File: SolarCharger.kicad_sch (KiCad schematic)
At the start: 28 parts, among them U5 ADM1176-1ARMZ-R7

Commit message: Local Stash
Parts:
- added R118: 0R, Resistor_SMD:R_0603_1608Metric, symbol Device:R_Small
- R56: value 0R -> 150k; MPN C844915 -> C402995
- R57: now not fitted; now left out of the parts list
- R58: value 126k -> 100k; now not fitted; now left out of the parts list
- R59: value 1.91M -> 2.32M
- R60: value 182k -> 143k
- R62: value 1.47M -> 2M
- R63: value 200k -> 270k
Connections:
- net MPPT/VCC: now also R118.1
- net MPPT/MPPC renamed MPPC
- net MPPC: now also R118.2
- no-connect marks 2 -> 1
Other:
- note added: "DNP if using MPPC"
- note added: "I2C ADDR R55, R56 +Z: DNP, 150k: 0x46"
- note added: "V_in(mppc) = 1.00 * (1 + R57 / R58) V_in(mppc) = 1.00 * (1 + 1.91M / 100k) V_in(mppc) = 1.00 * (1 + 19.1) V_in(mppc) = 20.1V"
- note added: "V_in(turnon) = 1.05 * (1 + R59 / R60) V_in(turnon) = 1.05 * (1 + 2.32M / 143k) V_in(turnon) = 1.05 * (1 + 16.22) V_in(turnon) = 18.08V"
- note added: "V_out = 1.00 * (1 + R62 / R63) V_out = 1.00 * (1 + 2M / 270k) V_out = 1.00 * (1 + 7.41) V_out = 8.41V"
- note removed: "I2C ADDR R55, R56 +Z: DNP, 0R: 0x42 Translated: 0x62"
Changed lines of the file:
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@@
 		(comment 2 "V. Kumar")
 	)
+	(text "V_in(mppc) = 1.00 * (1 + R57 / R58)\nV_in(mppc) = 1.00 * (1 + 1.91M / 100k)\nV_in(mppc) = 1.00 * (1 + 19.1)\nV_in(mppc) = 20.1V"
+		(exclude_from_sim no)
+		(at 18.288 94.996 0)
+		(effects
+			(font
+				(size 1.27 1.27)
+			)
+			(justify left)
+		)
+	)
 	(text "#TODO: Spec Fuses"
 		(exclude_from_sim no)
@@
 		)
 	)
+	(text "V_in(turnon) = 1.05 * (1 + R59 / R60)\nV_in(turnon) = 1.05 * (1 + 2.32M / 143k)\nV_in(turnon) = 1.05 * (1 + 16.22)\nV_in(turnon) = 18.08V"
+		(exclude_from_sim no)
+		(at 18.542 137.16 0)
+		(effects
+			(font
+				(size 1.27 1.27)
+			)
+			(justify left)
+		)
+	)
 	(text "Rsense"
 		(exclude_from_sim no)
@@
 		)
 	)
+	(text "V_out = 1.00 * (1 + R62 / R63)\nV_out = 1.00 * (1 + 2M / 270k)\nV_out = 1.00 * (1 + 7.41)\nV_out = 8.41V"
+		(exclude_from_sim no)
+		(at 116.84 116.586 0)
+		(effects
+			(font
+				(size 1.27 1.27)
+			)
+			(justify left)
+		)
+	)
 	(text "#TODO: Check Resistor Values"
 		(exclude_from_sim no)
@@
 		)
 	)
-	(text "I2C ADDR\nR55, R56\n+Z: DNP, 0R: 0x42\nTranslated: 0x62"
+	(text "DNP if using MPPC"
+		(exclude_from_sim no)
+		(at 93.726 125.73 0)
+		(effects
+			(font
+				(size 0.889 0.889)
+			)
+		)
+	)
+	(text "I2C ADDR\nR55, R56\n+Z: DNP, 150k: 0x46"
 		(exclude_from_sim no)
 		(at 181.356 91.948 0)
@@
 		(at 248.92 54.61)
 	)
-	(no_connect
-		(at 86.36 119.38)
-	)
 	(wire
 		(pts
@@
 	(wire
 		(pts
+			(xy 86.36 119.38) (xy 90.17 119.38)
+		)
+		(stroke
+			(width 0)
+			(type default)
+		)
+	)
+	(wire
+		(pts
 			(xy 133.35 53.34) (xy 133.35 59.69)
 		)
@@
 	(wire
 		(pts
+			(xy 95.25 119.38) (xy 100.33 119.38)
+		)
+		(stroke
+			(width 0)
+			(type default)
+		)
+	)
+	(wire
+		(pts
 			(xy 74.93 130.81) (xy 78.74 130.81)
 		)
@@
 		)
 	)
+	(label "MPPC"
+		(at 100.33 119.38 180)
+		(effects
+			(font
+				(size 0.889 0.889)
+			)
+			(justify right bottom)
+		)
+	)
 	(label "A1"
 		(at 243.84 78.74 180)
@@
 		)
 	)
+	(label "MPPC"
+		(at 54.61 111.76 0)
+		(effects
+			(font
+				(size 0.889 0.889)
+			)
+			(justify left bottom)
+		)
+	)
 	(label "PGOOD"
 		(at 86.36 105.41 0)
@@
 			)
 		)
-		(property "Value" "0R"
+		(property "Value" "150k"
 			(at 237.3479 84.968 0)
 			(effects
@@
 			)
 		)
-		(property "MPN" "C844915"
+		(property "MPN" "C402995"
 			(at 238.76 83.82 0)
 			(effects
@@
 		(unit 1)
 		(exclude_from_sim no)
-		(in_bom yes)
+		(in_bom no)
 		(on_board yes)
-		(dnp no)
+		(dnp yes)
 		(property "Reference" "R57"
 			(at 53.34 106.934 0)
@@
 			)
 		)
-		(property "Value" "1.91M"
+		(property "Value" "2.32M"
 			(at 68.58 135.128 90)
 			(effects
@@
 			)
 		)
-		(property "Value" "182k"
+		(property "Value" "143k"
 			(at 81.28 135.128 90)
 			(effects
@@
 	)
 	(symbol
+		(lib_id "Device:R_Small")
+		(at 92.71 119.38 90)
+		(unit 1)
+		(exclude_from_sim no)
+		(in_bom yes)
+		(on_board yes)
+		(dnp no)
+		(property "Reference" "R118"
+			(at 92.71 121.666 90)
+			(effects
+				(font
+					(size 1.27 1.27)
+				)
+			)
+		)
+		(property "Value" "0R"
+			(at 92.71 123.444 90)
+			(effects
+				(font
+					(size 1.27 1.27)
+				)
+			)
+		)
+		(property "Footprint" "Resistor_SMD:R_0603_1608Metric"
+			(at 92.71 119.38 0)
+			(effects
+				(font
+					(size 1.27 1.27)
+				)
+				(hide yes)
+			)
+		)
+		(property "Datasheet" "~"
+			(at 92.71 119.38 0)
+			(effects
+				(font
+					(size 1.27 1.27)
+				)
+				(hide yes)
+			)
+		)
+		(property "Description" "Resistor, small symbol"
+			(at 92.71 119.38 0)
+			(effects
+				(font
+					(size 1.27 1.27)
+				)
+				(hide yes)
+			)
+		)
+		(property "MPN" "C237792"
+			(at 92.71 119.38 90)
+			(effects
+				(font
+					(size 1.27 1.27)
+				)
+				(hide yes)
+			)
+		)
+		(pin "1"
+		)
+		(pin "2"
+		)
+		(instances
+			(project "+Z"
+				(path "/977a45af-b6d4-4b54-8e70-e74e2c44e8e7/3495d2a7-7425-4e27-a34a-beb5018fad2a"
+					(reference "R118")
+					(unit 1)
+				)
+			)
+		)
+	)
+	(symbol
 		(lib_id "Device:Solar_Cell")
 		(at 48.26 59.69 270)
@@
 			)
 		)
-		(property "Value" "200k"
+		(property "Value" "270k"
 			(at 106.68 117.856 0)
 			(effects
@@
 		(unit 1)
 		(exclude_from_sim no)
-		(in_bom yes)
+		(in_bom no)
 		(on_board yes)
-		(dnp no)
+		(dnp yes)
 		(property "Reference" "R58"
 			(at 53.34 114.554 0)
@@
 			)
 		)
-		(property "Value" "126k"
+		(property "Value" "100k"
 			(at 53.34 116.586 0)
 			(effects
@@
 			)
 		)
-		(property "Value" "1.47M"
+		(property "Value" "2M"
 			(at 106.68 107.696 0)
 			(effects

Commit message: V4 Updates
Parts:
- added H10, H11, H12, H13, H14, H15, H16, H17, H18, H19, H20, H9: MountingHole_Pad, TestPoint:TestPoint_Pad_D1.0mm, symbol Mechanical:MountingHole_Pad
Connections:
- net GND: now also H17.1, H18.1, H19.1, H20.1, H9.1
- net at D6.1 (K), F5.2, SC6.1 (+): now also H15.1
- net at D5.1 (K), D6.2 (A), SC5.1 (+)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: now also H14.1
- net at D3.1 (K), D4.2 (A), SC3.1 (+)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: now also H12.1, H16.1
- net at D2.1 (K), D3.2 (A), SC2.1 (+)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: now also H11.1
- net at D1.1 (K), D2.2 (A), SC1.1 (+)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: now also H10.1
- net at D4.1 (K), D5.2 (A), SC4.1 (+)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: now also H13.1
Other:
- moved on the sheet: R118, R57, R58, R59, R60, R61, R62, R63

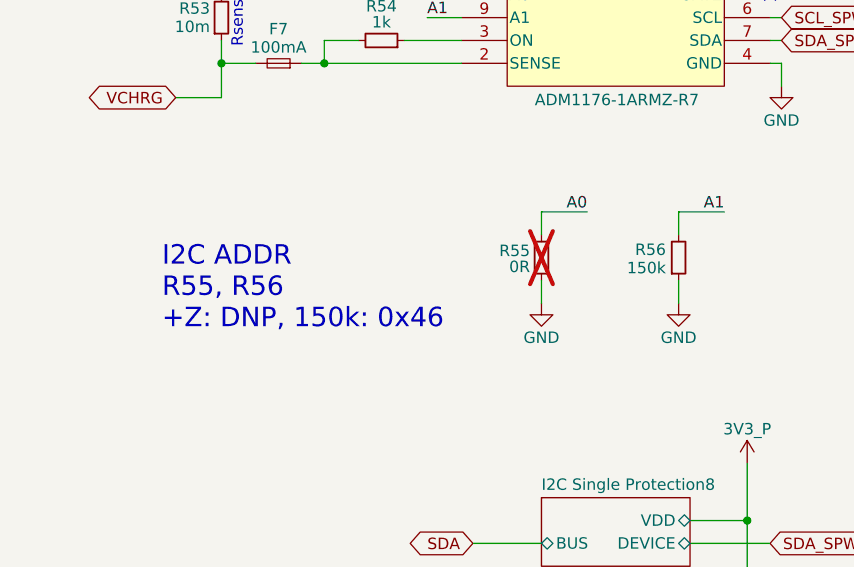
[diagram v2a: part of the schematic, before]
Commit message: Coil direction comment clarification
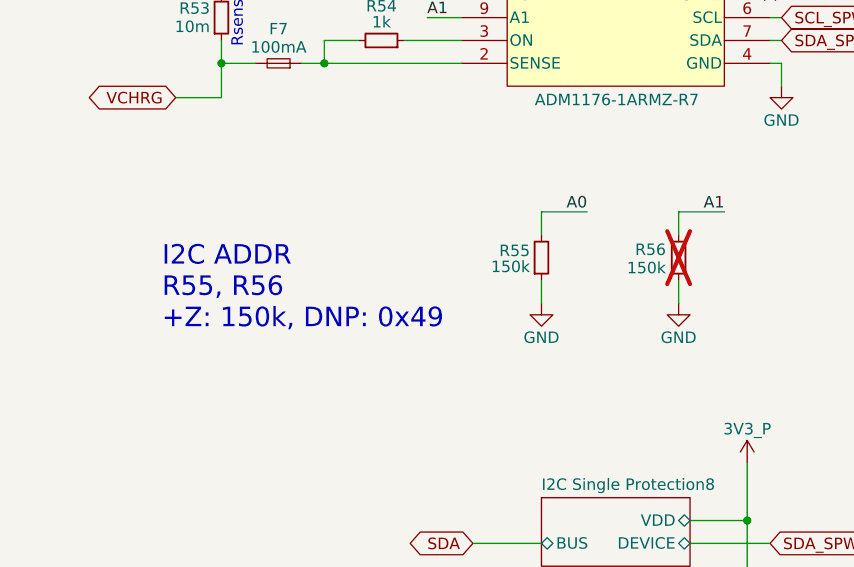
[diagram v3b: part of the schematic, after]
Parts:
- R55: value 0R -> 150k; now fitted; now in the parts list
- R56: now not fitted; now left out of the parts list
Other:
- note added: "I2C ADDR R55, R56 +Z: 150k, DNP: 0x49"
- note removed: "I2C ADDR R55, R56 +Z: DNP, 150k: 0x46"
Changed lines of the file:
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@@
 		)
 	)
-	(text "I2C ADDR\nR55, R56\n+Z: DNP, 150k: 0x46"
+	(text "I2C ADDR\nR55, R56\n+Z: 150k, DNP: 0x49"
 		(exclude_from_sim no)
 		(at 181.356 91.948 0)
@@
 		)
 		(instances
-			(project "Z+"
+			(project "+Z"
 				(path "/977a45af-b6d4-4b54-8e70-e74e2c44e8e7/3495d2a7-7425-4e27-a34a-beb5018fad2a"
 					(reference "R53")
@@
 		)
 		(instances
-			(project "Z+"
+			(project "+Z"
 				(path "/977a45af-b6d4-4b54-8e70-e74e2c44e8e7/3495d2a7-7425-4e27-a34a-beb5018fad2a"
 					(reference "#PWR057")
@@
 		)
 		(instances
-			(project "Z+"
+			(project "+Z"
 				(path "/977a45af-b6d4-4b54-8e70-e74e2c44e8e7/3495d2a7-7425-4e27-a34a-beb5018fad2a"
 					(reference "#PWR055")
@@
 		(unit 1)
 		(exclude_from_sim no)
-		(in_bom yes)
+		(in_bom no)
 		(on_board yes)
-		(dnp no)
+		(dnp yes)
 		(property "Reference" "R56"
 			(at 237.3479 82.936 0)
@@
 		)
 		(instances
-			(project "Z+"
+			(project "+Z"
 				(path "/977a45af-b6d4-4b54-8e70-e74e2c44e8e7/3495d2a7-7425-4e27-a34a-beb5018fad2a"
 					(reference "R56")
@@
 		)
 		(instances
-			(project "Z+"
+			(project "+Z"
 				(path "/977a45af-b6d4-4b54-8e70-e74e2c44e8e7/3495d2a7-7425-4e27-a34a-beb5018fad2a"
 					(reference "SC6")
@@
 		)
 		(instances
-			(project "Z+"
+			(project "+Z"
 				(path "/977a45af-b6d4-4b54-8e70-e74e2c44e8e7/3495d2a7-7425-4e27-a34a-beb5018fad2a"
 					(reference "R61")
@@
 		)
 		(instances
-			(project "Z+"
+			(project "+Z"
 				(path "/977a45af-b6d4-4b54-8e70-e74e2c44e8e7/3495d2a7-7425-4e27-a34a-beb5018fad2a"
 					(reference "#PWR042")
@@
 		)
 		(instances
-			(project "Z+"
+			(project "+Z"
 				(path "/977a45af-b6d4-4b54-8e70-e74e2c44e8e7/3495d2a7-7425-4e27-a34a-beb5018fad2a"
 					(reference "R57")
@@
 		)
 		(instances
-			(project "Z+"
+			(project "+Z"
 				(path "/977a45af-b6d4-4b54-8e70-e74e2c44e8e7/3495d2a7-7425-4e27-a34a-beb5018fad2a"
 					(reference "F5")
@@
 		)
 		(instances
-			(project "Z+"
+			(project "+Z"
 				(path "/977a45af-b6d4-4b54-8e70-e74e2c44e8e7/3495d2a7-7425-4e27-a34a-beb5018fad2a"
 					(reference "SC3")
@@
 		)
 		(instances
-			(project "Z+"
+			(project "+Z"
 				(path "/977a45af-b6d4-4b54-8e70-e74e2c44e8e7/3495d2a7-7425-4e27-a34a-beb5018fad2a"
 					(reference "D1")
@@
 		)
 		(instances
-			(project "Z+"
+			(project "+Z"
 				(path "/977a45af-b6d4-4b54-8e70-e74e2c44e8e7/3495d2a7-7425-4e27-a34a-beb5018fad2a"
 					(reference "R59")
@@
 		)
 		(instances
-			(project "Z+"
+			(project "+Z"
 				(path "/977a45af-b6d4-4b54-8e70-e74e2c44e8e7/3495d2a7-7425-4e27-a34a-beb5018fad2a"
 					(reference "D5")
@@
 		)
 		(instances
-			(project "Z+"
+			(project "+Z"
 				(path "/977a45af-b6d4-4b54-8e70-e74e2c44e8e7/3495d2a7-7425-4e27-a34a-beb5018fad2a"
 					(reference "D6")
@@
 		)
 		(instances
-			(project "Z+"
+			(project "+Z"
 				(path "/977a45af-b6d4-4b54-8e70-e74e2c44e8e7/3495d2a7-7425-4e27-a34a-beb5018fad2a"
 					(reference "SC4")
@@
 		)
 		(instances
-			(project "Z+"
+			(project "+Z"
 				(path "/977a45af-b6d4-4b54-8e70-e74e2c44e8e7/3495d2a7-7425-4e27-a34a-beb5018fad2a"
 					(reference "R60")
@@
 		(unit 1)
 		(exclude_from_sim no)
-		(in_bom no)
+		(in_bom yes)
 		(on_board yes)
-		(dnp yes)
+		(dnp no)
 		(property "Reference" "R55"
 			(at 222.25 83.058 0)
@@
 			)
 		)
-		(property "Value" "0R"
+		(property "Value" "150k"
 			(at 222.25 84.836 0)
 			(effects
@@
 		)
 		(instances
-			(project "Z+"
+			(project "+Z"
 				(path "/977a45af-b6d4-4b54-8e70-e74e2c44e8e7/3495d2a7-7425-4e27-a34a-beb5018fad2a"
 					(reference "R55")
@@
 		)
 		(instances
-			(project "Z+"
+			(project "+Z"
 				(path "/977a45af-b6d4-4b54-8e70-e74e2c44e8e7/3495d2a7-7425-4e27-a34a-beb5018fad2a"
 					(reference "#PWR040")
@@
 		)
 		(instances
-			(project "Z+"
+			(project "+Z"
 				(path "/977a45af-b6d4-4b54-8e70-e74e2c44e8e7/3495d2a7-7425-4e27-a34a-beb5018fad2a"
 					(reference "SC2")
@@
 		)
 		(instances
-			(project "Z+"
+			(project "+Z"
 				(path "/977a45af-b6d4-4b54-8e70-e74e2c44e8e7/3495d2a7-7425-4e27-a34a-beb5018fad2a"
 					(reference "SC1")
@@
 		)
 		(instances
-			(project "Z+"
+			(project "+Z"
 				(path "/977a45af-b6d4-4b54-8e70-e74e2c44e8e7/3495d2a7-7425-4e27-a34a-beb5018fad2a"
 					(reference "#PWR058")
@@
 		)
 		(instances
-			(project "Z+"
+			(project "+Z"
 				(path "/977a45af-b6d4-4b54-8e70-e74e2c44e8e7/3495d2a7-7425-4e27-a34a-beb5018fad2a"
 					(reference "D3")
@@
 		)
 		(instances
-			(project "Z+"
+			(project "+Z"
 				(path "/977a45af-b6d4-4b54-8e70-e74e2c44e8e7/3495d2a7-7425-4e27-a34a-beb5018fad2a"
 					(reference "D4")
@@
 		)
 		(instances
-			(project "Z+"
+			(project "+Z"
 				(path "/977a45af-b6d4-4b54-8e70-e74e2c44e8e7/3495d2a7-7425-4e27-a34a-beb5018fad2a"
 					(reference "#PWR045")
@@
 		)
 		(instances
-			(project "Z+"
+			(project "+Z"
 				(path "/977a45af-b6d4-4b54-8e70-e74e2c44e8e7/3495d2a7-7425-4e27-a34a-beb5018fad2a"
 					(reference "R63")
@@
 		)
 		(instances
-			(project "Z+"
+			(project "+Z"
 				(path "/977a45af-b6d4-4b54-8e70-e74e2c44e8e7/3495d2a7-7425-4e27-a34a-beb5018fad2a"
 					(reference "R58")
@@
 		)
 		(instances
-			(project "Z+"
+			(project "+Z"
 				(path "/977a45af-b6d4-4b54-8e70-e74e2c44e8e7/3495d2a7-7425-4e27-a34a-beb5018fad2a"
 					(reference "SC5")
@@
 		)
 		(instances
-			(project "Z+"
+			(project "+Z"
 				(path "/977a45af-b6d4-4b54-8e70-e74e2c44e8e7/3495d2a7-7425-4e27-a34a-beb5018fad2a"
 					(reference "D2")
@@
 		)
 		(instances
-			(project "Z+"
+			(project "+Z"
 				(path "/977a45af-b6d4-4b54-8e70-e74e2c44e8e7/3495d2a7-7425-4e27-a34a-beb5018fad2a"
 					(reference "F7")
@@
 		)
 		(instances
-			(project "Z+"
+			(project "+Z"
 				(path "/977a45af-b6d4-4b54-8e70-e74e2c44e8e7/3495d2a7-7425-4e27-a34a-beb5018fad2a"
 					(reference "R62")
@@
 		)
 		(instances
-			(project "Z+"
+			(project "+Z"
 				(path "/977a45af-b6d4-4b54-8e70-e74e2c44e8e7/3495d2a7-7425-4e27-a34a-beb5018fad2a"
 					(reference "#PWR041")
@@
 		)
 		(instances
-			(project "Z+"
+			(project "+Z"
 				(path "/977a45af-b6d4-4b54-8e70-e74e2c44e8e7/3495d2a7-7425-4e27-a34a-beb5018fad2a"
 					(reference "C13")
@@
 		)
 		(instances
-			(project "Z+"
+			(project "+Z"
 				(path "/977a45af-b6d4-4b54-8e70-e74e2c44e8e7/3495d2a7-7425-4e27-a34a-beb5018fad2a"
 					(reference "F6")
@@
 		)
 		(instances
-			(project "Z+"
+			(project "+Z"
 				(path "/977a45af-b6d4-4b54-8e70-e74e2c44e8e7/3495d2a7-7425-4e27-a34a-beb5018fad2a"
 					(reference "#PWR046")
@@
 		)
 		(instances
-			(project "Z+"
+			(project "+Z"
 				(path "/977a45af-b6d4-4b54-8e70-e74e2c44e8e7/3495d2a7-7425-4e27-a34a-beb5018fad2a"
 					(reference "#SUPPLY08")
@@
 		)
 		(instances
-			(project "Z+"
+			(project "+Z"
 				(path "/977a45af-b6d4-4b54-8e70-e74e2c44e8e7/3495d2a7-7425-4e27-a34a-beb5018fad2a"
 					(reference "U5")
@@
 		)
 		(instances
-			(project "Z+"
+			(project "+Z"
 				(path "/977a45af-b6d4-4b54-8e70-e74e2c44e8e7/3495d2a7-7425-4e27-a34a-beb5018fad2a"
 					(reference "R54")
